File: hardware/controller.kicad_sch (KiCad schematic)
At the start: 7 parts, among them Q3 BC847BS, U1 LPS28DFW, U3 Seeed-ESP32C3

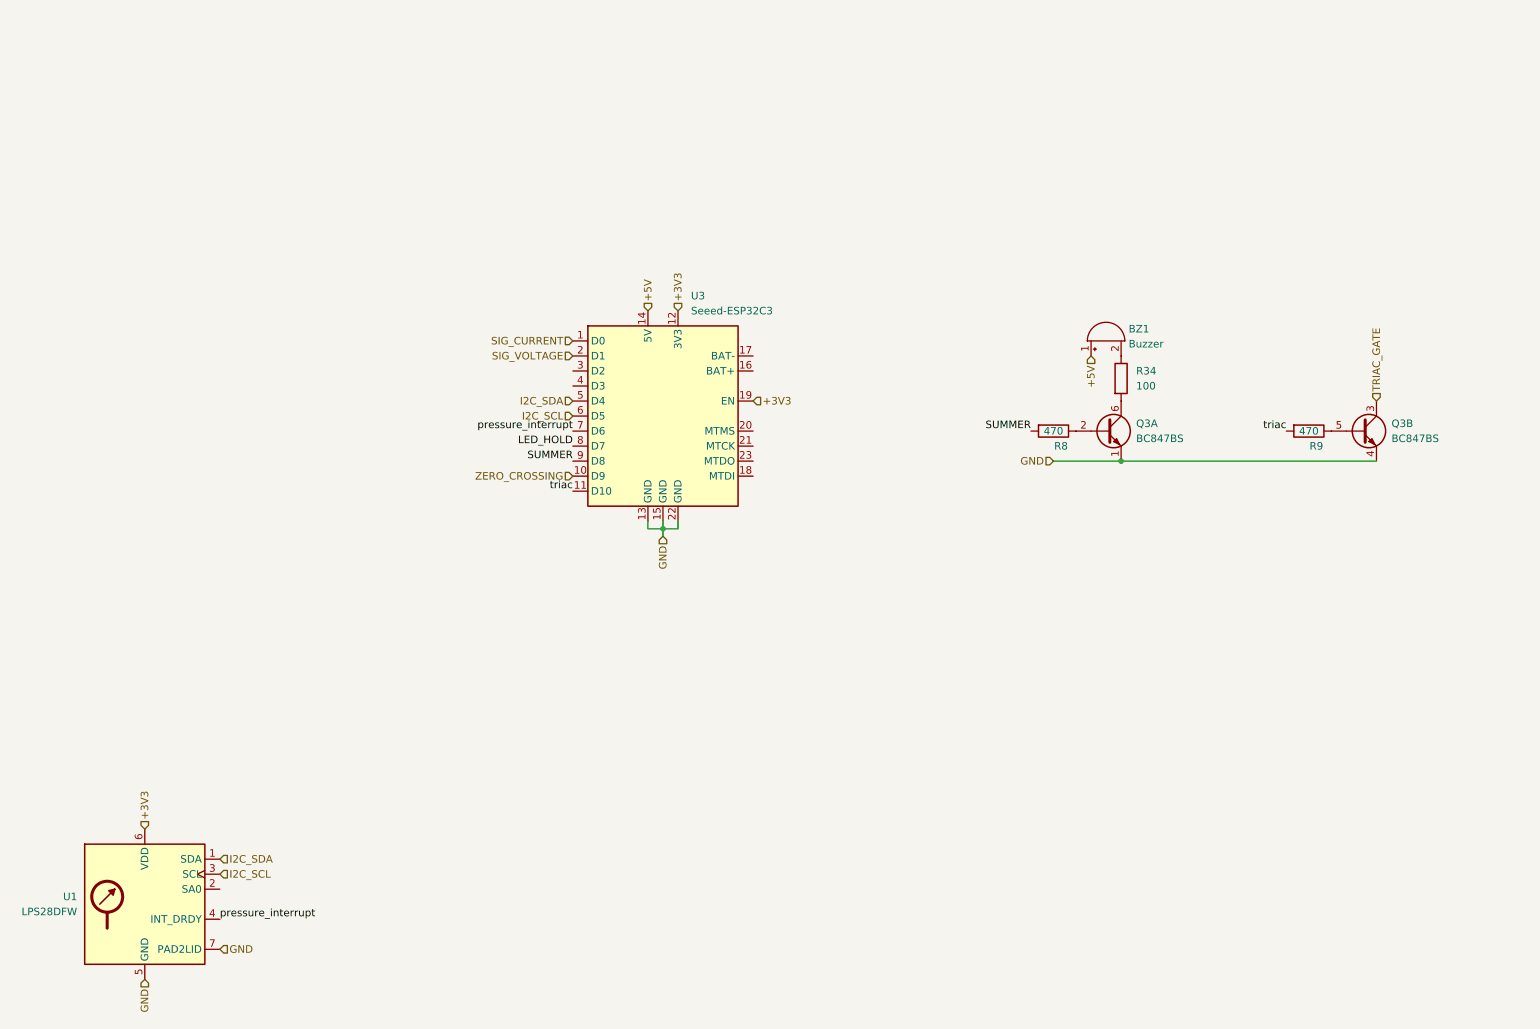
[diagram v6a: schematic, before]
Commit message: added testpoints. adjusted opamps for correct measurement. replaced hard resistors with potentiometer trimmers if necessary
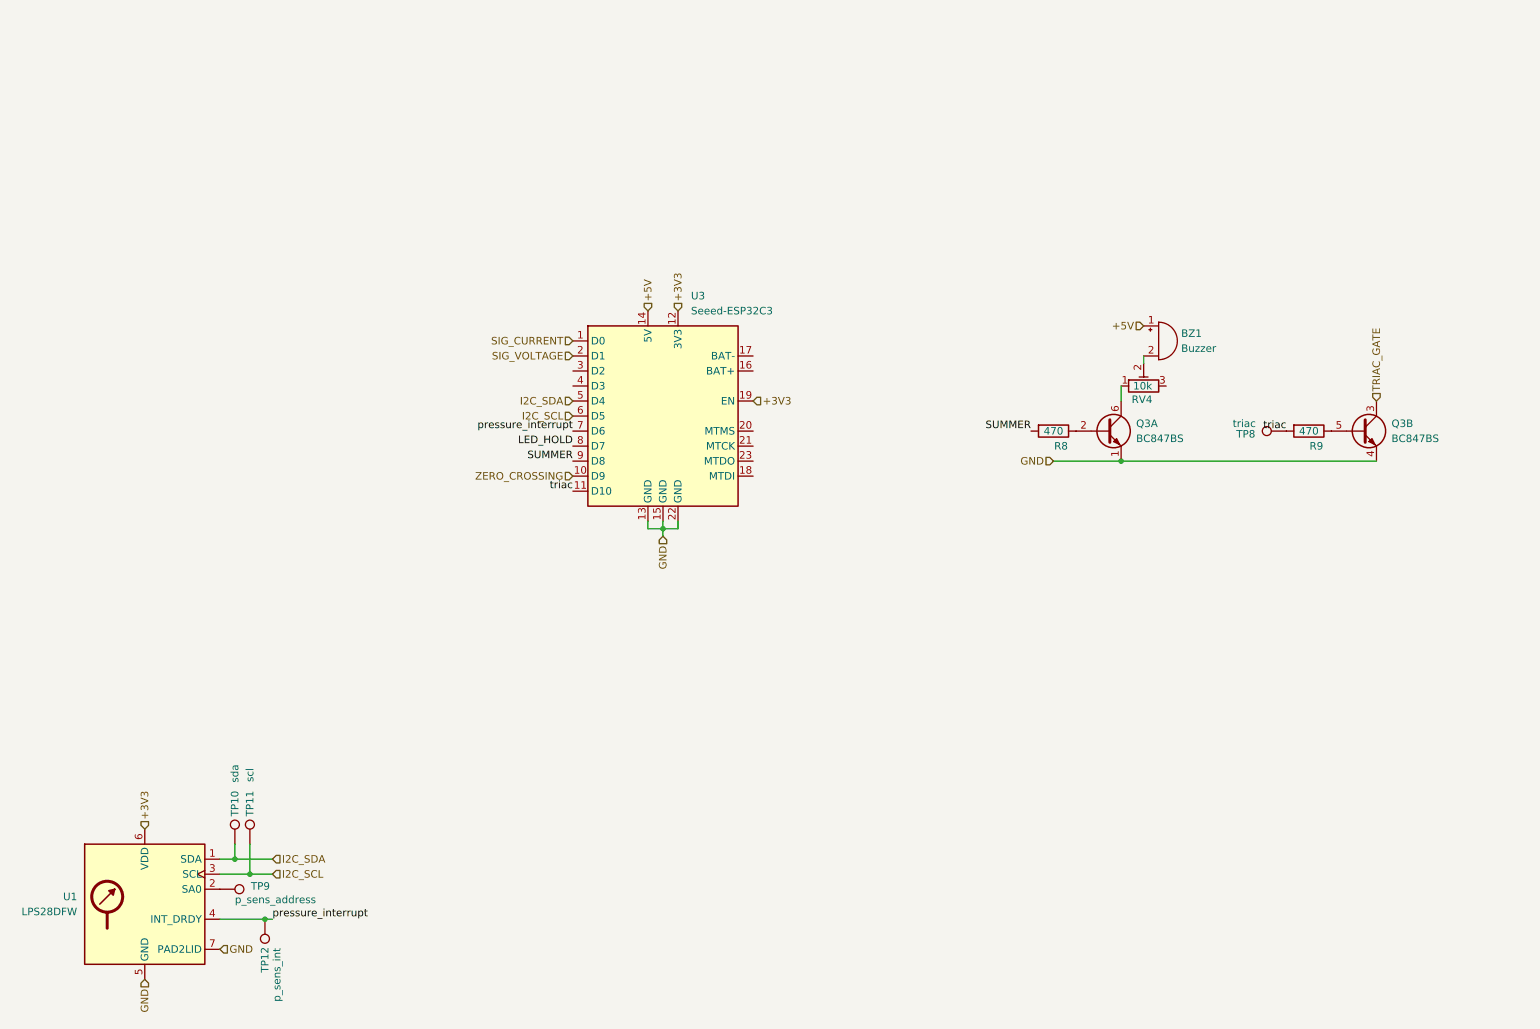
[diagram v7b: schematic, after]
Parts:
- removed R34: 100, Resistor_SMD:R_0603_1608Metric, symbol Device:R
- added RV4: 10k, Potentiometer_THT:Potentiometer_Bourns_3299W_Vertical, symbol Device:R_Potentiometer_Trim
- added TP10: sda, TestPoint:TestPoint_Pad_D1.0mm, symbol Connector:TestPoint
- added TP11: scl, TestPoint:TestPoint_Pad_D1.0mm, symbol Connector:TestPoint
- added TP12: p_sens_int, TestPoint:TestPoint_Pad_D1.0mm, symbol Connector:TestPoint
- added TP8: triac, TestPoint:TestPoint_Pad_D1.0mm, symbol Connector:TestPoint
- added TP9: p_sens_address, TestPoint:TestPoint_Pad_D1.0mm, symbol Connector:TestPoint
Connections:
- net I2C_SCL: now also TP11.1
- net I2C_SDA: now also TP10.1
- net pressure_interrupt: now also TP12.1
- net triac: now also TP8.1
- net at BZ1.2 (+): now also RV4.2
- net at U1.2 (SA0): now also TP9.1
- net at Q3.6 (C1): now also RV4.1
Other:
- moved on the sheet: BZ1

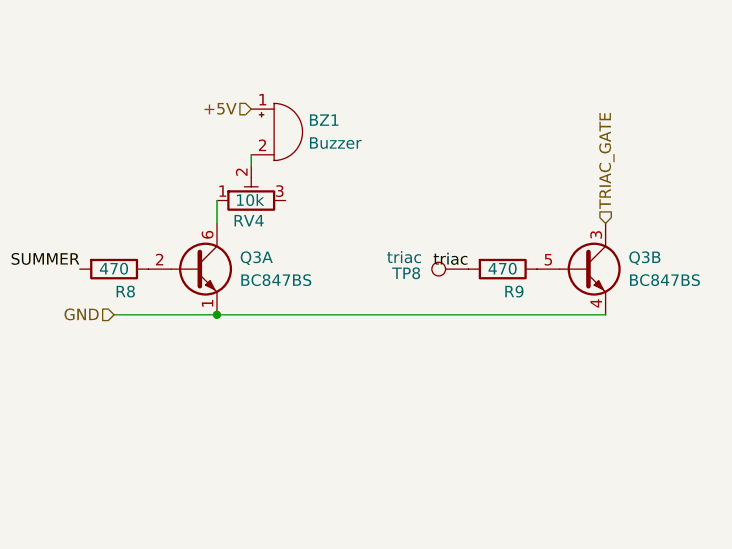
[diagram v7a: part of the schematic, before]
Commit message: changed opamp for a rail-to-rail device. bugfix: got the right package for phoenix mstba outlets. beauty: rearranged some test points for better visibility. bugfix: added bypass diodes to analog output to protect adc on chip
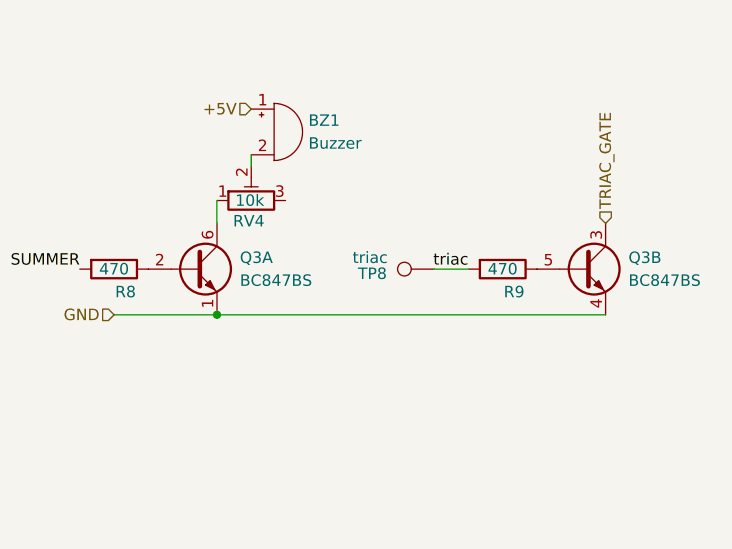
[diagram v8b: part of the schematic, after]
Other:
- moved on the sheet: TP8
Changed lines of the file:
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@@
+	(wire
+		(pts
+			(xy 233.68 91.44) (xy 237.49 91.44)
+		)
+		(stroke
+			(width 0)
+			(type default)
+		)
+	)
 	(wire
 		(pts
@@
 	(symbol
 		(lib_id "Connector:TestPoint")
-		(at 237.49 91.44 90)
+		(at 233.68 91.44 90)
 		(unit 1)
 		(exclude_from_sim no)
@@
 		(dnp no)
 		(property "Reference" "TP8"
-			(at 230.632 91.948 90)
+			(at 226.822 91.948 90)
 			(effects
 				(font
@@
 		)
 		(property "Value" "triac"
-			(at 230.378 90.17 90)
+			(at 226.568 90.17 90)
 			(effects
 				(font
@@
 		)
 		(property "Footprint" "TestPoint:TestPoint_Pad_D1.0mm"
-			(at 237.49 86.36 0)
+			(at 233.68 86.36 0)
 			(effects
 				(font
@@
 		)
 		(property "Datasheet" "~"
-			(at 237.49 86.36 0)
+			(at 233.68 86.36 0)
 			(effects
 				(font
@@
 		)
 		(property "Description" "test point"
-			(at 237.49 91.44 0)
-			(effects
-				(font
+			(at 233.68 91.44 0)
+			(effects
+				(font
